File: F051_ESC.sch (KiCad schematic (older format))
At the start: 12 parts, among them J1 Conn_01x02, J2 Conn_01x04, J3 Conn_01x04, J4 Conn_01x03, J5 Conn_01x01, J6 Conn_01x02

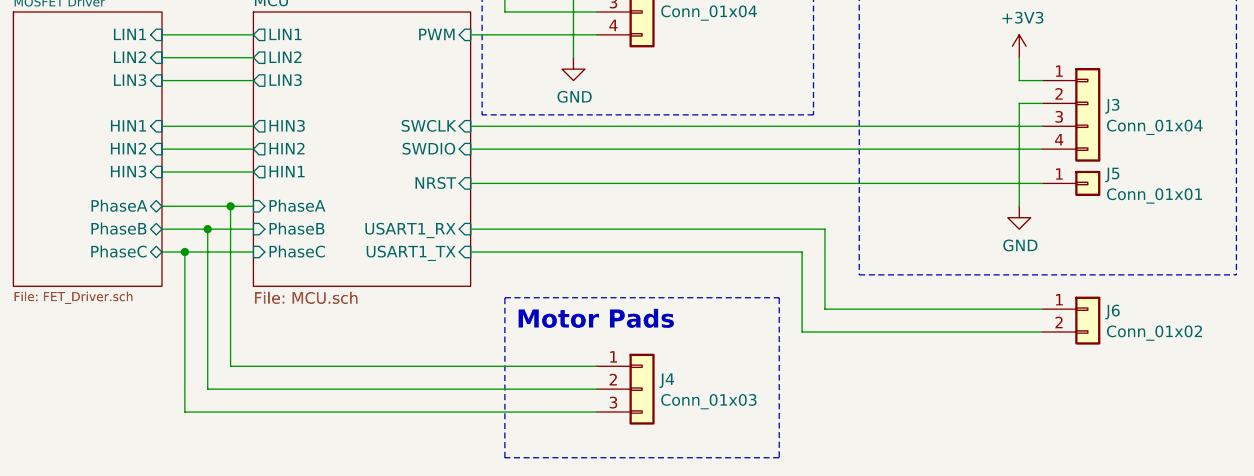
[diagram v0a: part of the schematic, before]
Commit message: Rerouting of a lot of layers
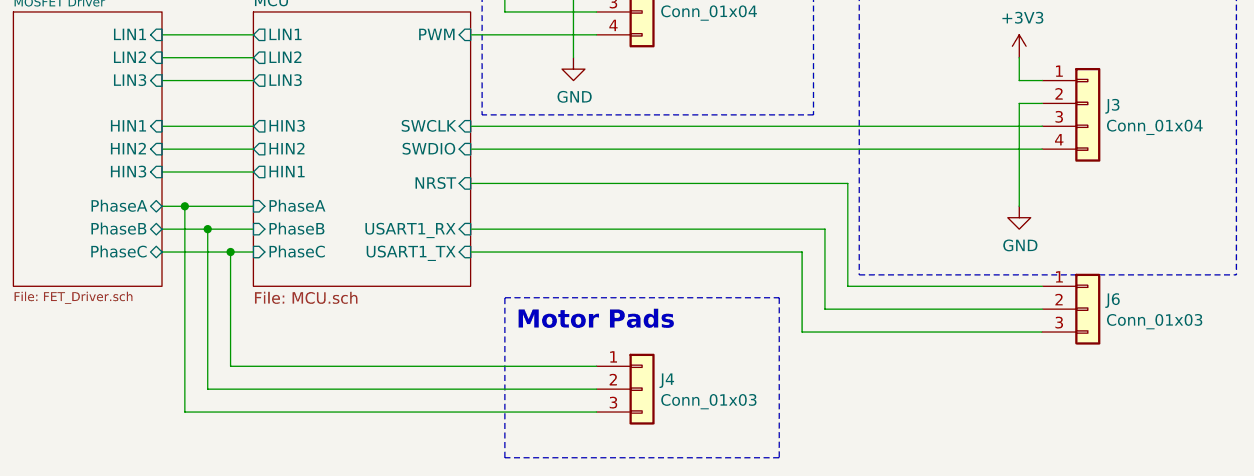
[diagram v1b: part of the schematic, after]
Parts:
- removed J5: Conn_01x01, Connector_PinHeader_2.54mm:PinHeader_1x01_P2.54mm_Vertical, symbol Connector_Generic:Conn_01x01
- removed J6: Conn_01x02, Connector_PinHeader_2.54mm:PinHeader_1x02_P2.54mm_Vertical, symbol Connector_Generic:Conn_01x02
- added J6: Conn_01x03, Connector_PinHeader_2.54mm:PinHeader_1x03_P2.54mm_Vertical, symbol Connector_Generic:Conn_01x03
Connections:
- net MCU/NRST: now also J6.1 (Pin_1)
- net MCU/PhaseA: now also J4.3 (Pin_3); no longer J4.1 (Pin_1)
- net MCU/PhaseC: now also J4.1 (Pin_1); no longer J4.3 (Pin_3)
- net MCU/USART1_RX: now also J6.2 (Pin_2)
- net MCU/USART1_TX: now also J6.3 (Pin_3)
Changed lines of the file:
@@
 Wire Wire Line
 	4050 4400 4450 4400
-Wire Wire Line
-	4050 4650 4250 4650
-Wire Wire Line
-	4050 4750 4150 4750
 $Comp
 L power:GND #PWR0114
@@
 	1    0    0    -1
 $EndComp
-Wire Wire Line
-	4350 4550 4350 5250
-Wire Wire Line
-	4350 5250 5950 5250
-Connection ~ 4350 4550
-Wire Wire Line
-	4350 4550 4450 4550
-Wire Wire Line
-	4250 5350 5950 5350
-Wire Wire Line
-	5950 5450 4150 5450
-Wire Wire Line
-	4050 4550 4350 4550
-Wire Wire Line
-	4250 4650 4250 5350
-Connection ~ 4250 4650
-Wire Wire Line
-	4250 4650 4450 4650
-Wire Wire Line
-	4150 4750 4150 5450
-Connection ~ 4150 4750
-Wire Wire Line
-	4150 4750 4450 4750
 $Comp
 L Device:C_Small C16
@@
 F16 "USART1_RX" I R 5400 4650 50
 $EndSheet
-$Comp
-L Connector_Generic:Conn_01x01 J5
-U 1 1 603DA1F9
-P 8100 4450
-F 0 "J5" H 8180 4492 50  0000 L CNN
-F 1 "Conn_01x01" H 8180 4401 50  0000 L CNN
-F 2 "Connector_PinHeader_2.54mm:PinHeader_1x01_P2.54mm_Vertical" H 8100 4450 50  0001 C CNN
-F 3 "~" H 8100 4450 50  0001 C CNN
-	1    8100 4450
-	1    0    0    -1
-$EndComp
 Wire Notes Line
 	8750 3500 7100 3500
@@
 	7900 4300 5400 4300
 Wire Wire Line
-	5400 4450 7900 4450
-$Comp
-L Connector_Generic:Conn_01x02 J6
-U 1 1 604C1457
+	6950 4650 6950 5000
+Wire Wire Line
+	6950 5000 7900 5000
+Wire Wire Line
+	7900 5100 6850 5100
+Wire Wire Line
+	6850 5100 6850 4750
+Wire Wire Line
+	6850 4750 5400 4750
+Wire Wire Line
+	5400 4650 6950 4650
+$Comp
+L Connector_Generic:Conn_01x03 J6
+U 1 1 6051CE43
 P 8100 5000
-F 0 "J6" H 8180 4992 50  0000 L CNN
-F 1 "Conn_01x02" H 8180 4901 50  0000 L CNN
-F 2 "Connector_PinHeader_2.54mm:PinHeader_1x02_P2.54mm_Vertical" H 8100 5000 50  0001 C CNN
+F 0 "J6" H 8180 5042 50  0000 L CNN
+F 1 "Conn_01x03" H 8180 4951 50  0000 L CNN
+F 2 "Connector_PinHeader_2.54mm:PinHeader_1x03_P2.54mm_Vertical" H 8100 5000 50  0001 C CNN
 F 3 "~" H 8100 5000 50  0001 C CNN
 	1    8100 5000
@@
 $EndComp
 Wire Wire Line
-	6950 4650 6950 5000
-Wire Wire Line
-	6950 5000 7900 5000
-Wire Wire Line
-	7900 5100 6850 5100
-Wire Wire Line
-	6850 5100 6850 4750
-Wire Wire Line
-	6850 4750 5400 4750
-Wire Wire Line
-	5400 4650 6950 4650
+	5400 4450 7050 4450
+Wire Wire Line
+	7050 4450 7050 4900
+Wire Wire Line
+	7050 4900 7900 4900
+Wire Wire Line
+	4050 4750 4350 4750
+Wire Wire Line
+	4050 4550 4150 4550
+Wire Wire Line
+	4050 4650 4250 4650
+Wire Wire Line
+	4150 4550 4150 5450
+Wire Wire Line
+	4150 5450 5950 5450
+Connection ~ 4150 4550
+Wire Wire Line
+	4150 4550 4450 4550
+Wire Wire Line
+	5950 5350 4250 5350
+Wire Wire Line
+	4250 5350 4250 4650
+Connection ~ 4250 4650
+Wire Wire Line
+	4250 4650 4450 4650
+Wire Wire Line
+	4350 4750 4350 5250
+Wire Wire Line
+	4350 5250 5950 5250
+Connection ~ 4350 4750
+Wire Wire Line
+	4350 4750 4450 4750
 $EndSCHEMATC
